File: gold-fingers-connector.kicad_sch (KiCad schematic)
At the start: 128 parts, among them J1 Socket_DC-SCM-2.1_2x84_Rev-1-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

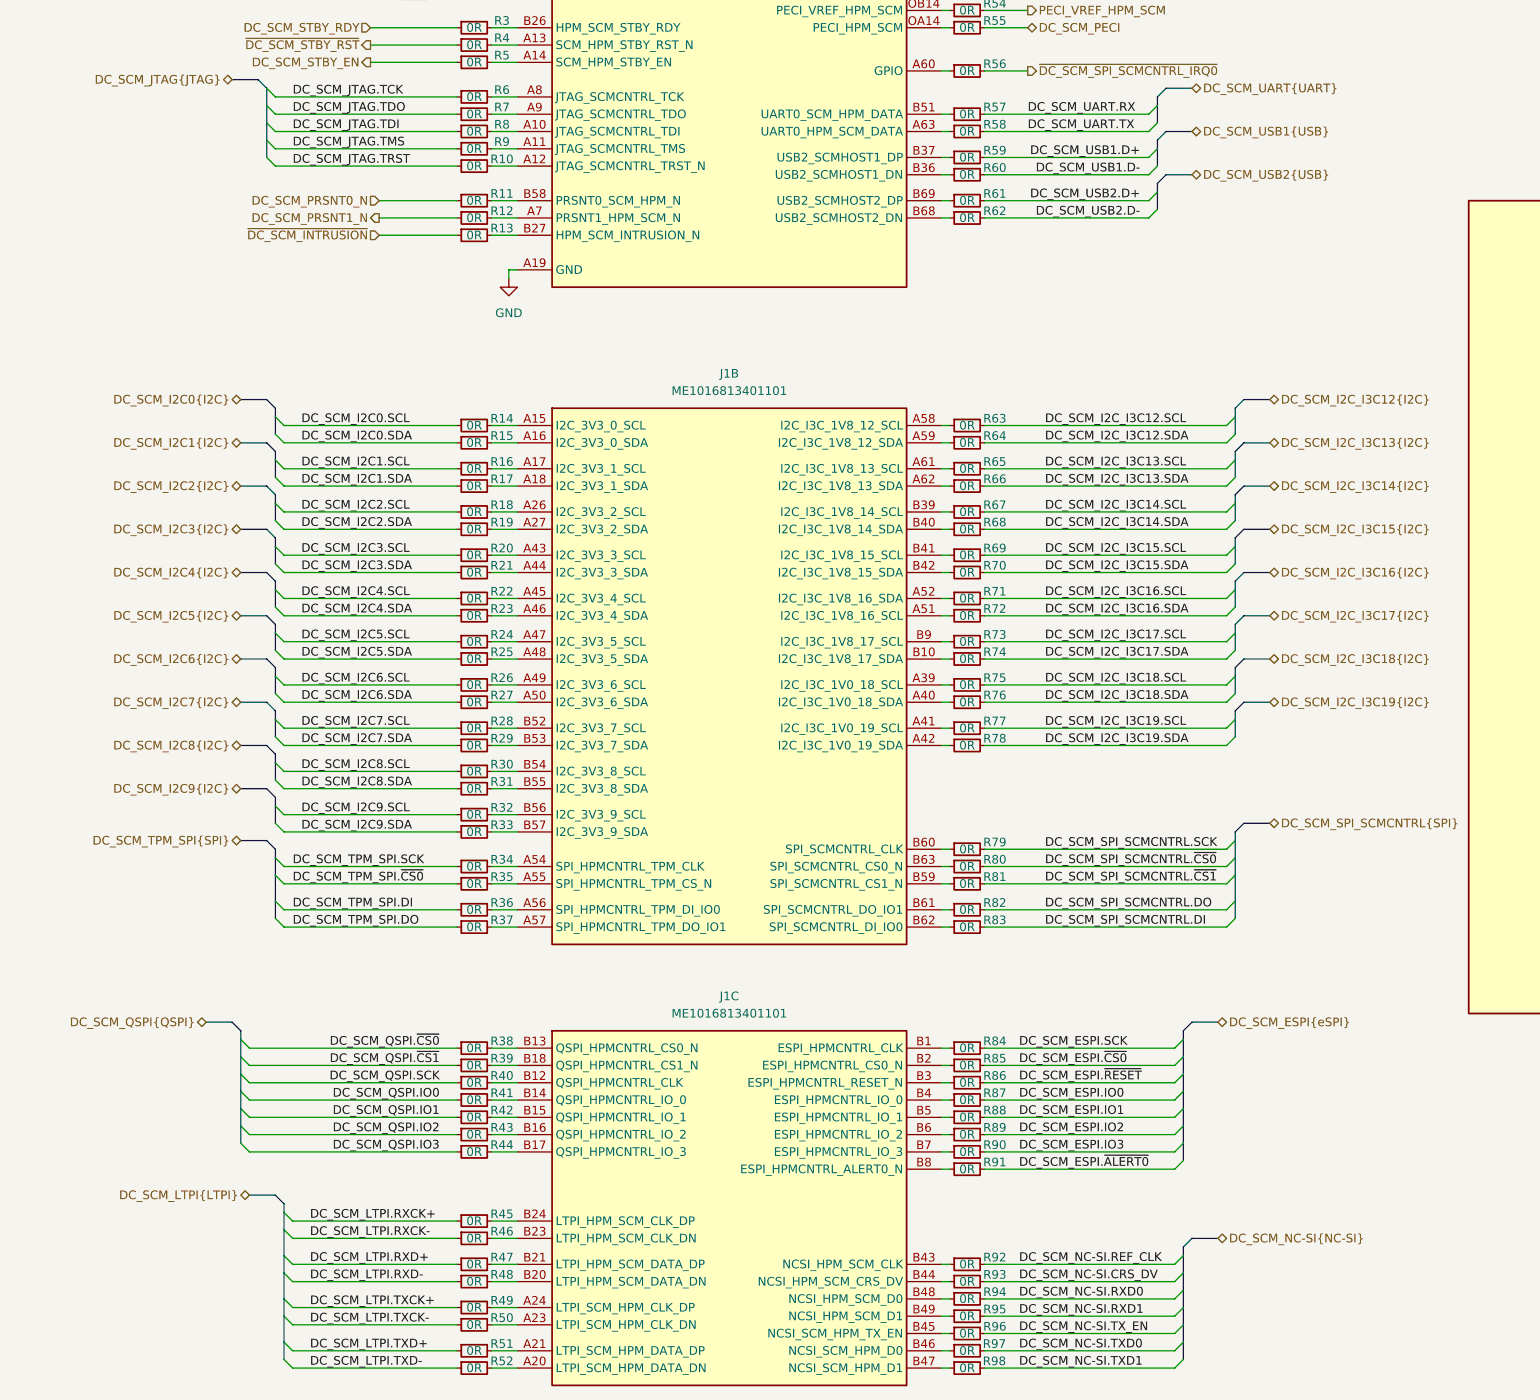
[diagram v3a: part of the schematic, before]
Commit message: [#100720] Start placing silkscreen labels
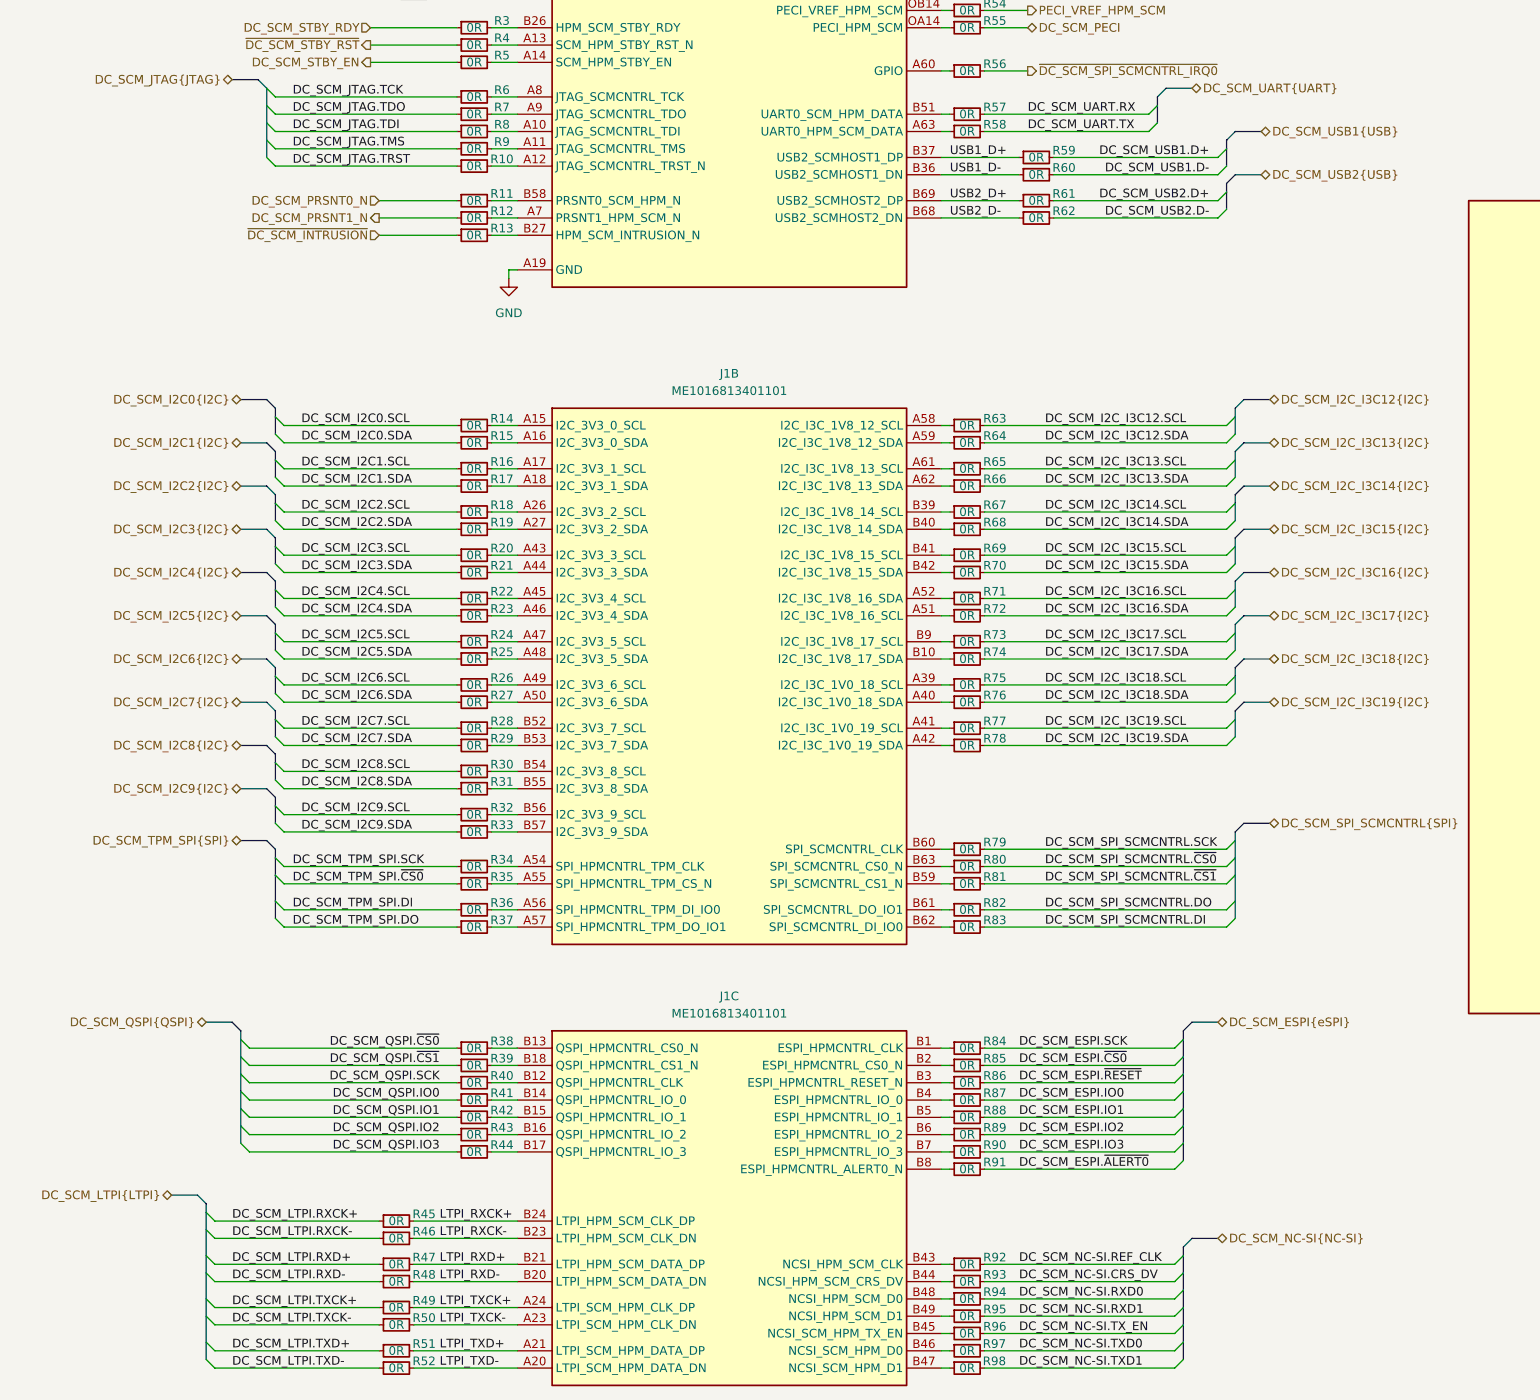
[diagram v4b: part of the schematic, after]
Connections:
- net LTPI_RXCK-: now reaches J1.B23 (LTPI_HPM_SCM_CLK_DN), R46.2
- net LTPI_TXD-: now reaches J1.A20 (LTPI_SCM_HPM_DATA_DN), R52.2
- net LTPI_TXD+: now reaches J1.A21 (LTPI_SCM_HPM_DATA_DP), R51.2
- net LTPI_TXCK-: now reaches J1.A23 (LTPI_SCM_HPM_CLK_DN), R50.2
- net LTPI_TXCK+: now reaches J1.A24 (LTPI_SCM_HPM_CLK_DP), R49.2
- net LTPI_RXD-: now reaches J1.B20 (LTPI_HPM_SCM_DATA_DN), R48.2
- net LTPI_RXD+: now reaches J1.B21 (LTPI_HPM_SCM_DATA_DP), R47.2
- net LTPI_RXCK+: now reaches J1.B24 (LTPI_HPM_SCM_CLK_DP), R45.2
- net USB1_D-: now reaches J1.B36 (USB2_SCMHOST1_DN), R60.1
- net USB1_D+: now reaches J1.B37 (USB2_SCMHOST1_DP), R59.1
- net USB2_D-: now reaches J1.B68 (USB2_SCMHOST2_DN), R62.1
- net USB2_D+: now reaches J1.B69 (USB2_SCMHOST2_DP), R61.1
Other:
- moved on the sheet: R45, R46, R47, R48, R49, R50, R51, R52, R59, R60, R61, R62

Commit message: [#100720] Finish silkscreen
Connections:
- net CLK_100M_1_CLK+: no longer J1.A68 (PCIE_HPM_SCM_CLK_100M_1_S0_DN), R103.1
- new net CLK_100M_1_CLK-: J1.A68 (PCIE_HPM_SCM_CLK_100M_1_S0_DN), R103.1
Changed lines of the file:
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@@
 		)
 	)
-	(label "CLK_100M_1_CLK+"
+	(label "CLK_100M_1_CLK-"
 		(at 281.94 92.71 0)
 		(effects

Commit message: [#100720] Route power
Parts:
- removed R1: R_0R_0402, antmicro-footprints:R_0402_1005Metric, symbol antmicroResistors0402:R_0R_0402
- added R1: R_0R_22.4A_0603, antmicro-footprints:R_0603_1608Metric, symbol antmicroResistors0603:R_0R_22.4A_0603
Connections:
- net DC_SCM_12V_AUX: now also R1.1
- net 12V_AUX: now reaches J1.A1 (P12V_AUX), J1.A2 (P12V_AUX), J1.A3 (P12V_AUX), J1.A4 (P12V_AUX)
- net 12V_AUX: now also R1.2
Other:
- moved on the sheet: R2

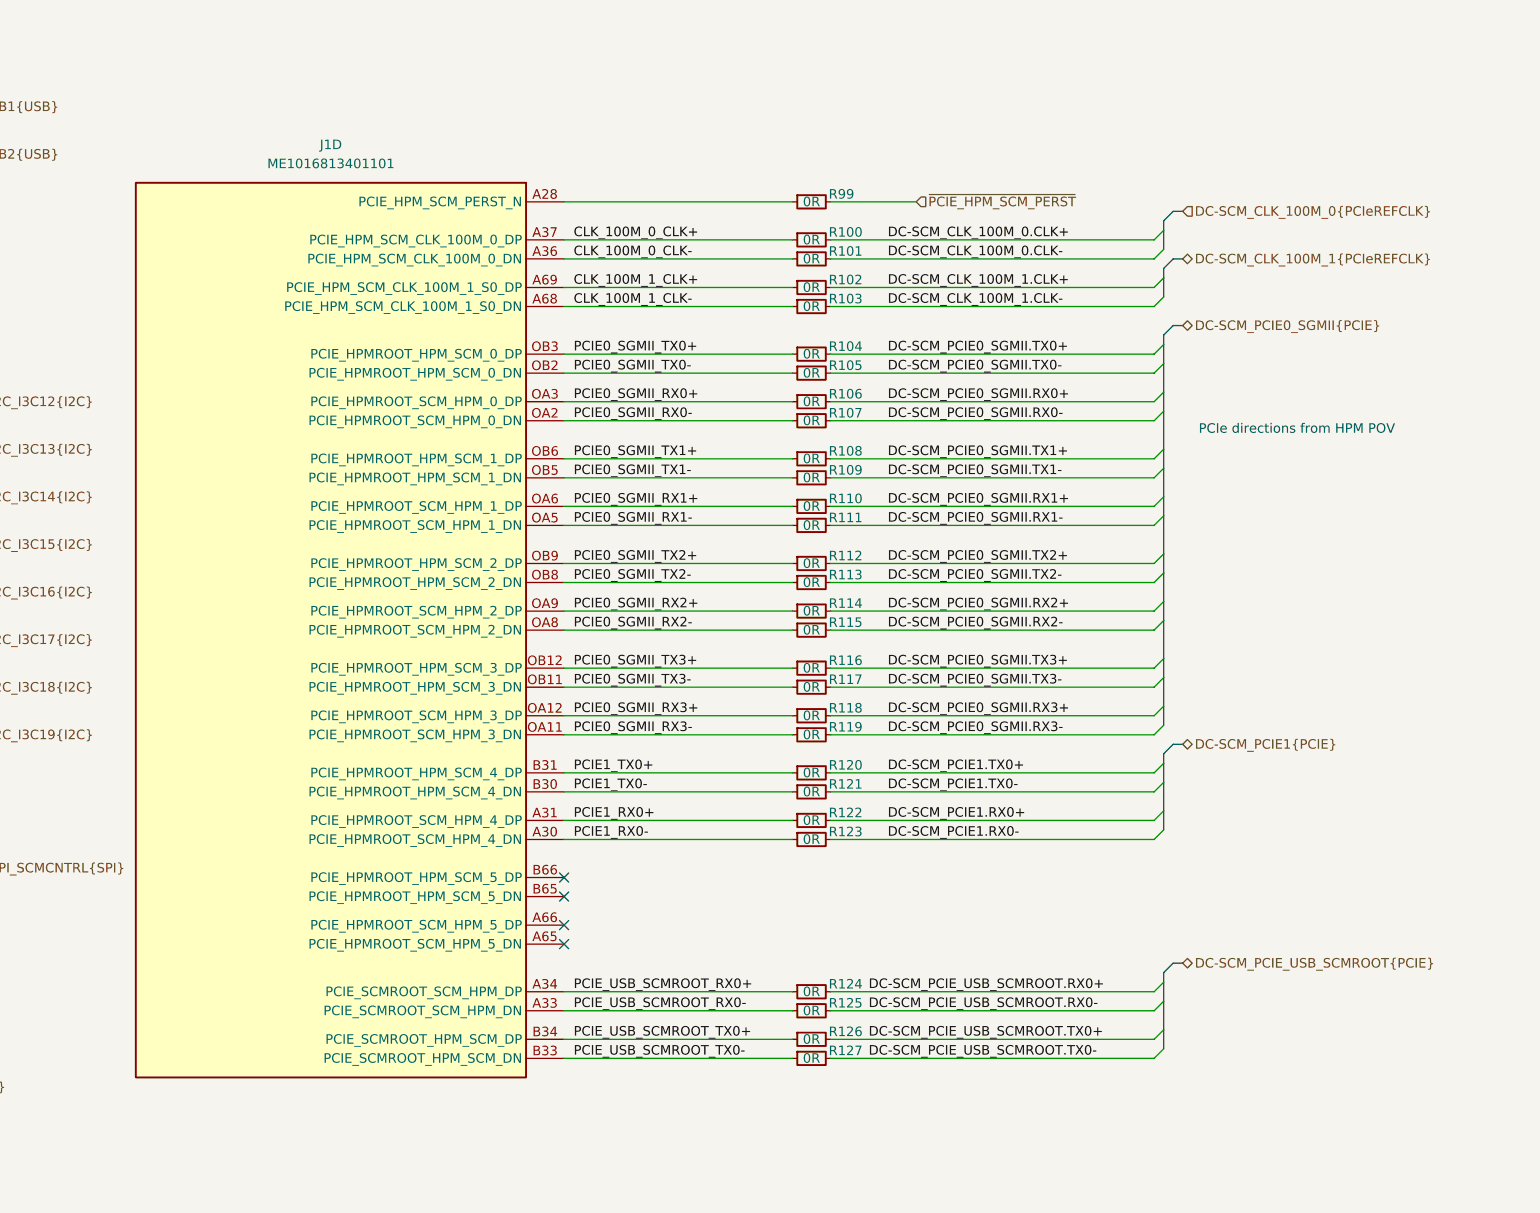
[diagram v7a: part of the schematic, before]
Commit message: [#100720] Finish schematic after PCIe to USB addition
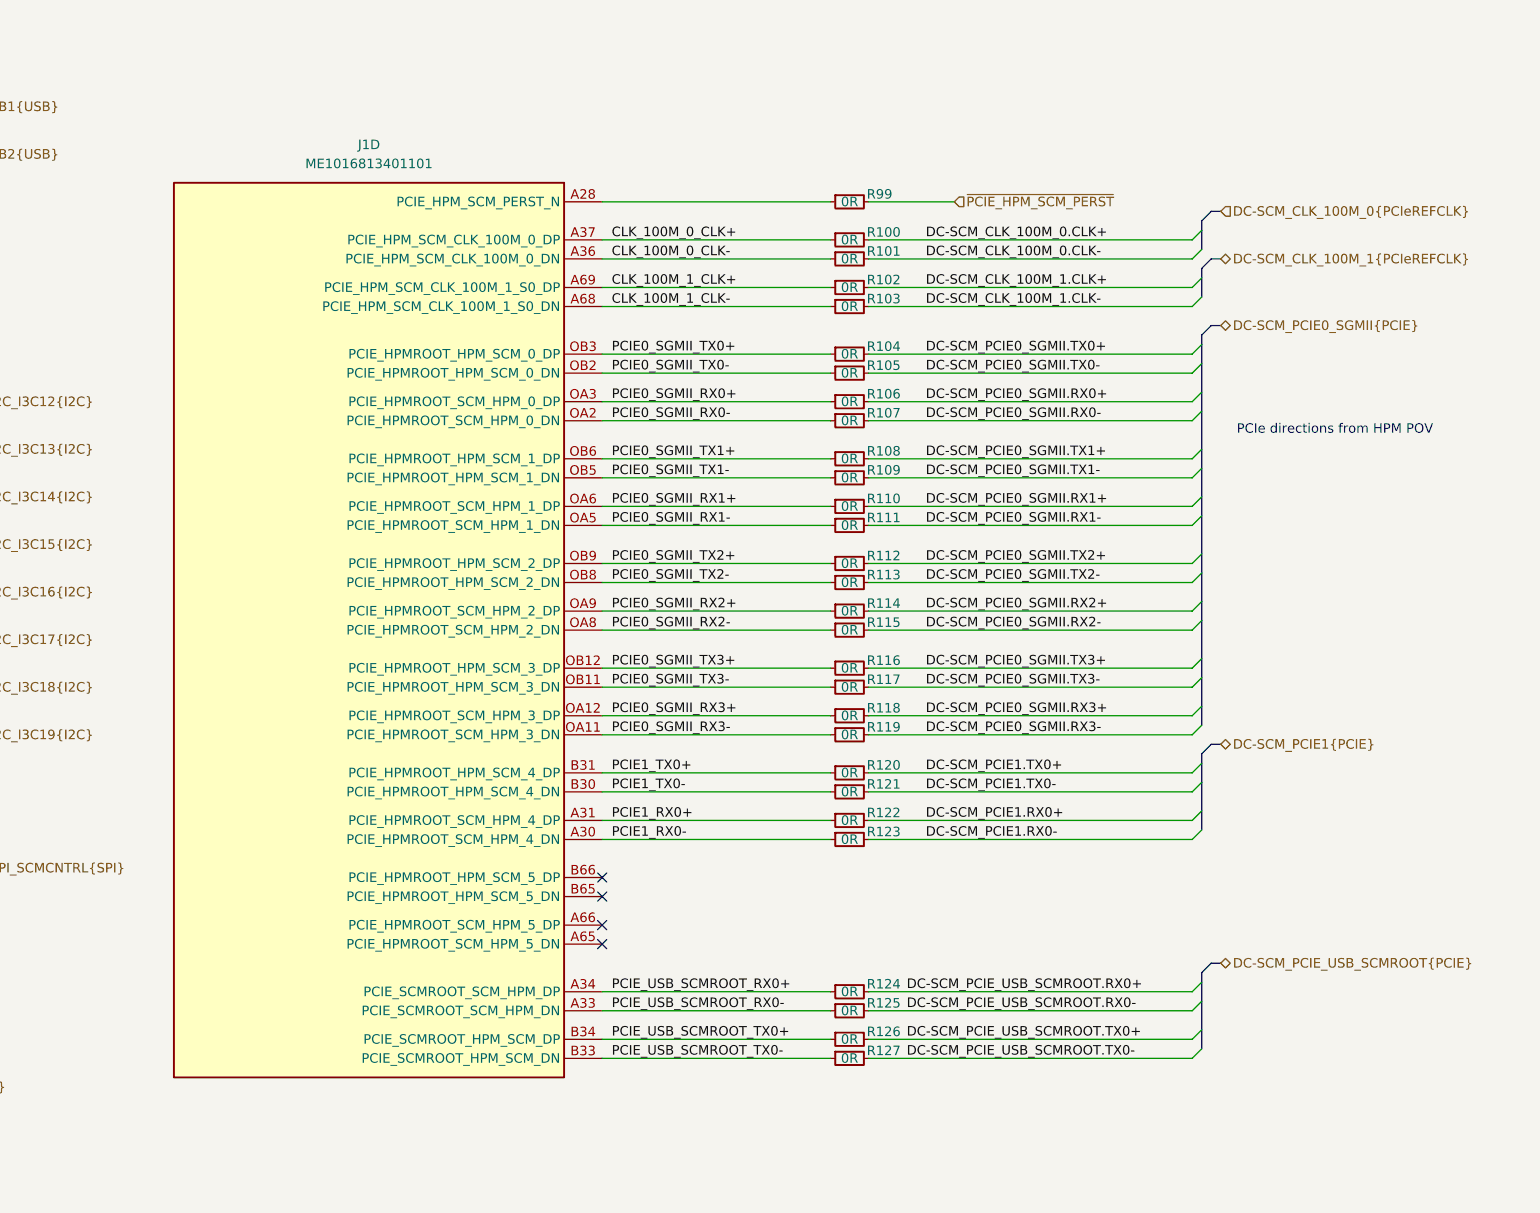
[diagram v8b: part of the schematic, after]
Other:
- moved on the sheet: J1D, R100, R101, R102, R103, R104, R105, R106, R107, R108, R109, R110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
